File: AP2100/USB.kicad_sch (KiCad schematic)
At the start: 42 parts, among them IC10 MAX1564ETE+, J10 SS-52000-001, J8 SS-52000-001, J9 SS-52000-001, U22 74LVC2G04, U23 SP3011, U24 SP3011, U25 SP3011, U7 LS1043ASE7xxx

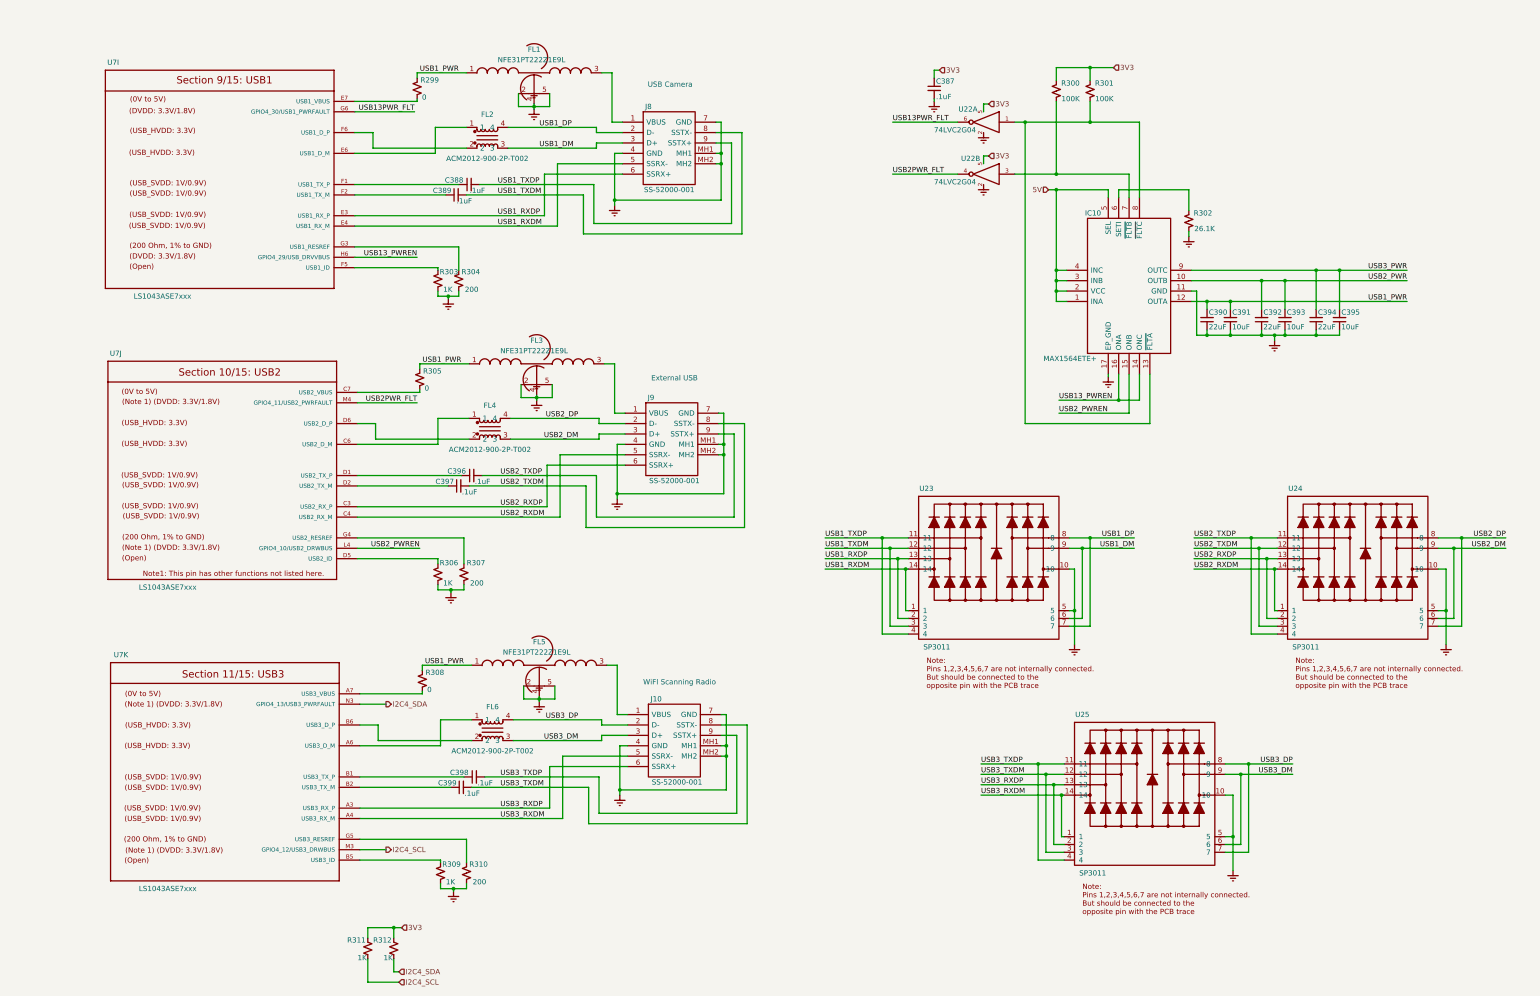
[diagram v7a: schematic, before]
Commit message: More cleanups - fix incorrect serial console pinout Add netclasses
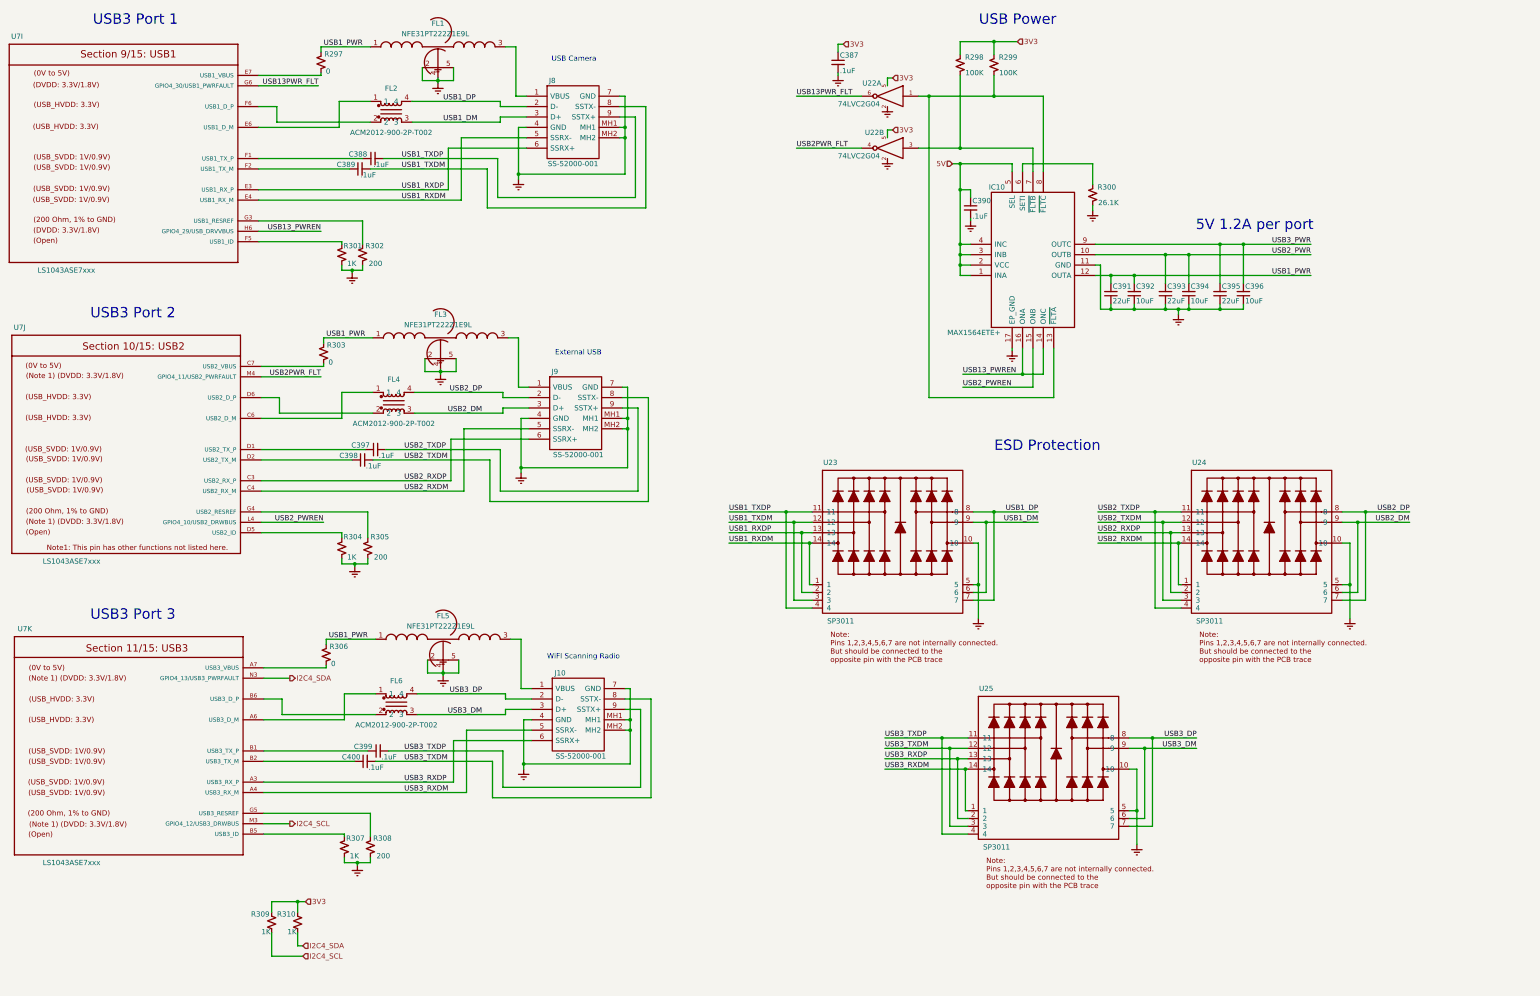
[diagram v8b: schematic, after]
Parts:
- added C390: .1uF, Capacitor_SMD:C_0402_1005Metric, symbol Device:C_Small
- renumbered C390 to C391, C391 to C392, C392 to C393, C393 to C394, C394 to C395, C395 to C396, C396 to C397, C397 to C398, C398 to C399, C399 to C400, R299 to R297, R300 to R298, R301 to R299, R302 to R300, R303 to R301, R304 to R302, R305 to R303, R306 to R304, R307 to R305, R308 to R306, R309 to R307, R310 to R308, R311 to R309, R312 to R310
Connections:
- net 5V: now also C390.1
- net GND: now also C390.2
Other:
- note added: "5V 1.2A per port"
- note added: "ESD Protection"
- note added: "USB Power"
- note added: "USB3 Port 1"
- note added: "USB3 Port 2"
- note added: "USB3 Port 3"
- company: IS ImageStream Internet Solutions, Inc. -> ISis ImageStream Internet Solutions, Inc.
- moved on the sheet: C387, C388, C389, C391, C392, C393, C394, C395, C396, C397, C398, C399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
